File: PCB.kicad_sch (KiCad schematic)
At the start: 29 parts

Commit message: HALMET redesign
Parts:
- removed C1001, C1002, C1003, C1004, C1005, C1006, C1007, C1008, C1009, C1010, C1011, C1012, C1013, C1014, C1015, C1016, C1017, C1018, C1019, C1020, C1021, C1022, C1023, C1024, C1025, C1027, C1028: 100nF, Capacitor_SMD:C_0402_1005Metric, symbol Device:C
- added G501: CC-BY, HALMET:cc-by_5mm, symbol Graphic:SYM_Radioactive_Radiation_Small
- added G502: CE-logo, Symbol:CE-Logo_11.2x8mm_SilkScreen, symbol Graphic:SYM_Radioactive_Radiation_Small
- added G503: WEEE-logo, Symbol:WEEE-Logo_5.6x8mm_SilkScreen, symbol Graphic:SYM_Radioactive_Radiation_Small
- added G504: OSHW-logo, Symbol:OSHW-Logo2_9.8x8mm_SilkScreen, symbol Graphic:SYM_Radioactive_Radiation_Small
- added G505: HL-Logo, HALMET:Hat_Labs_25.4mm, symbol Graphic:SYM_Radioactive_Radiation_Small
- added G505: HL-Pictogram, HALMET:HaL_picto_8mm, symbol Graphic:SYM_Radioactive_Radiation_Small
- H1001, H1002: footprint SH-ESP32:MountingSlot_3.2mm_M3_Unplated -> HALMET:MountingSlot_3.2mm_M3_Unplated
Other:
- note removed: "Decoupling caps"
- title: Sailor Hat with ESP32 -> Hat Labs Marine Engine/Tank interface (HALMET)

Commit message: Implement HALMET v1.0.0 design changes
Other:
- title: Hat Labs Marine Engine/Tank interface (HALMET) -> Hat Labs Marine Engine & Tank interface (HALMET)
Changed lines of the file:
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@@
   (paper "A4")
   (title_block
-    (title "Hat Labs Marine Engine/Tank interface (HALMET)")
-    (date "2023-09-19")
-    (rev "1.0.0-a1")
+    (title "Hat Labs Marine Engine & Tank interface (HALMET)")
+    (date "2023-11-27")
+    (rev "1.0.0")
     (company "Hat Labs Ltd")
     (comment 1 "https://creativecommons.org/licenses/by-sa/4.0")
@@
   )
   (symbol (lib_id "Graphic:SYM_Radioactive_Radiation_Small") (at 160.02 55.88 0) (unit 1)
-    (in_bom no) (on_board no) (dnp no) (fields_autoplaced)
+    (in_bom no) (on_board yes) (dnp no) (fields_autoplaced)
     (property "Reference" "G502" (at 163.83 54.2925 0)
       (effects (font (size 1.27 1.27)) (justify left))

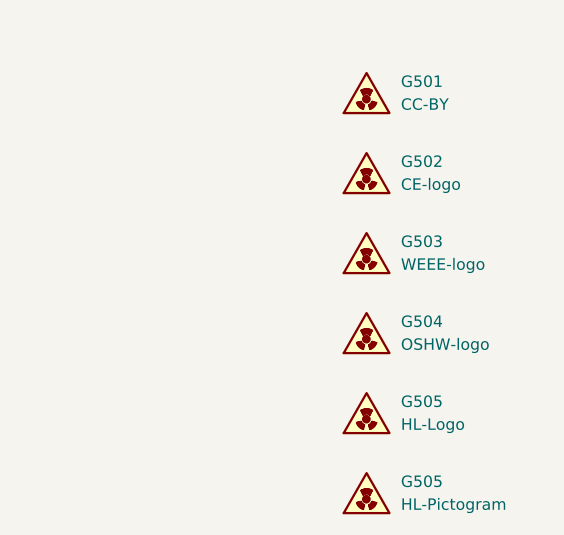
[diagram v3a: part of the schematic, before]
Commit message: Save with a newer KiCad; change parts for availability; fix rotations
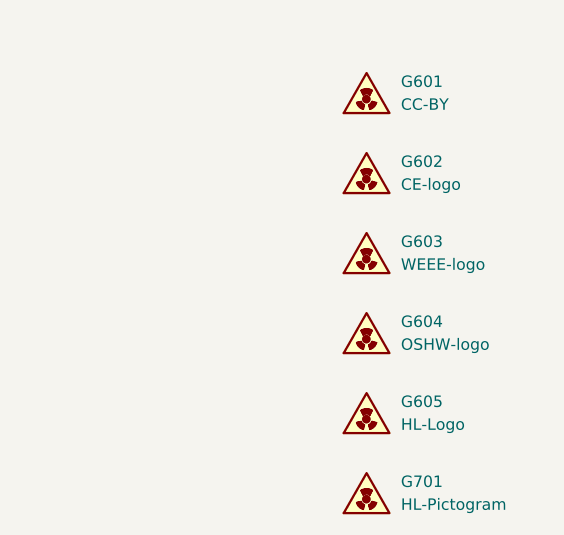
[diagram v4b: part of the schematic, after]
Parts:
- renumbered G501 to G601, G502 to G602, G503 to G603, G504 to G604, G505 to G605, G505 to G701
